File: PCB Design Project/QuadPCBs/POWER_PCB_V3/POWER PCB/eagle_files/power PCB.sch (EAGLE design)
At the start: 33 parts, among them U2 LM2678DX-5.0

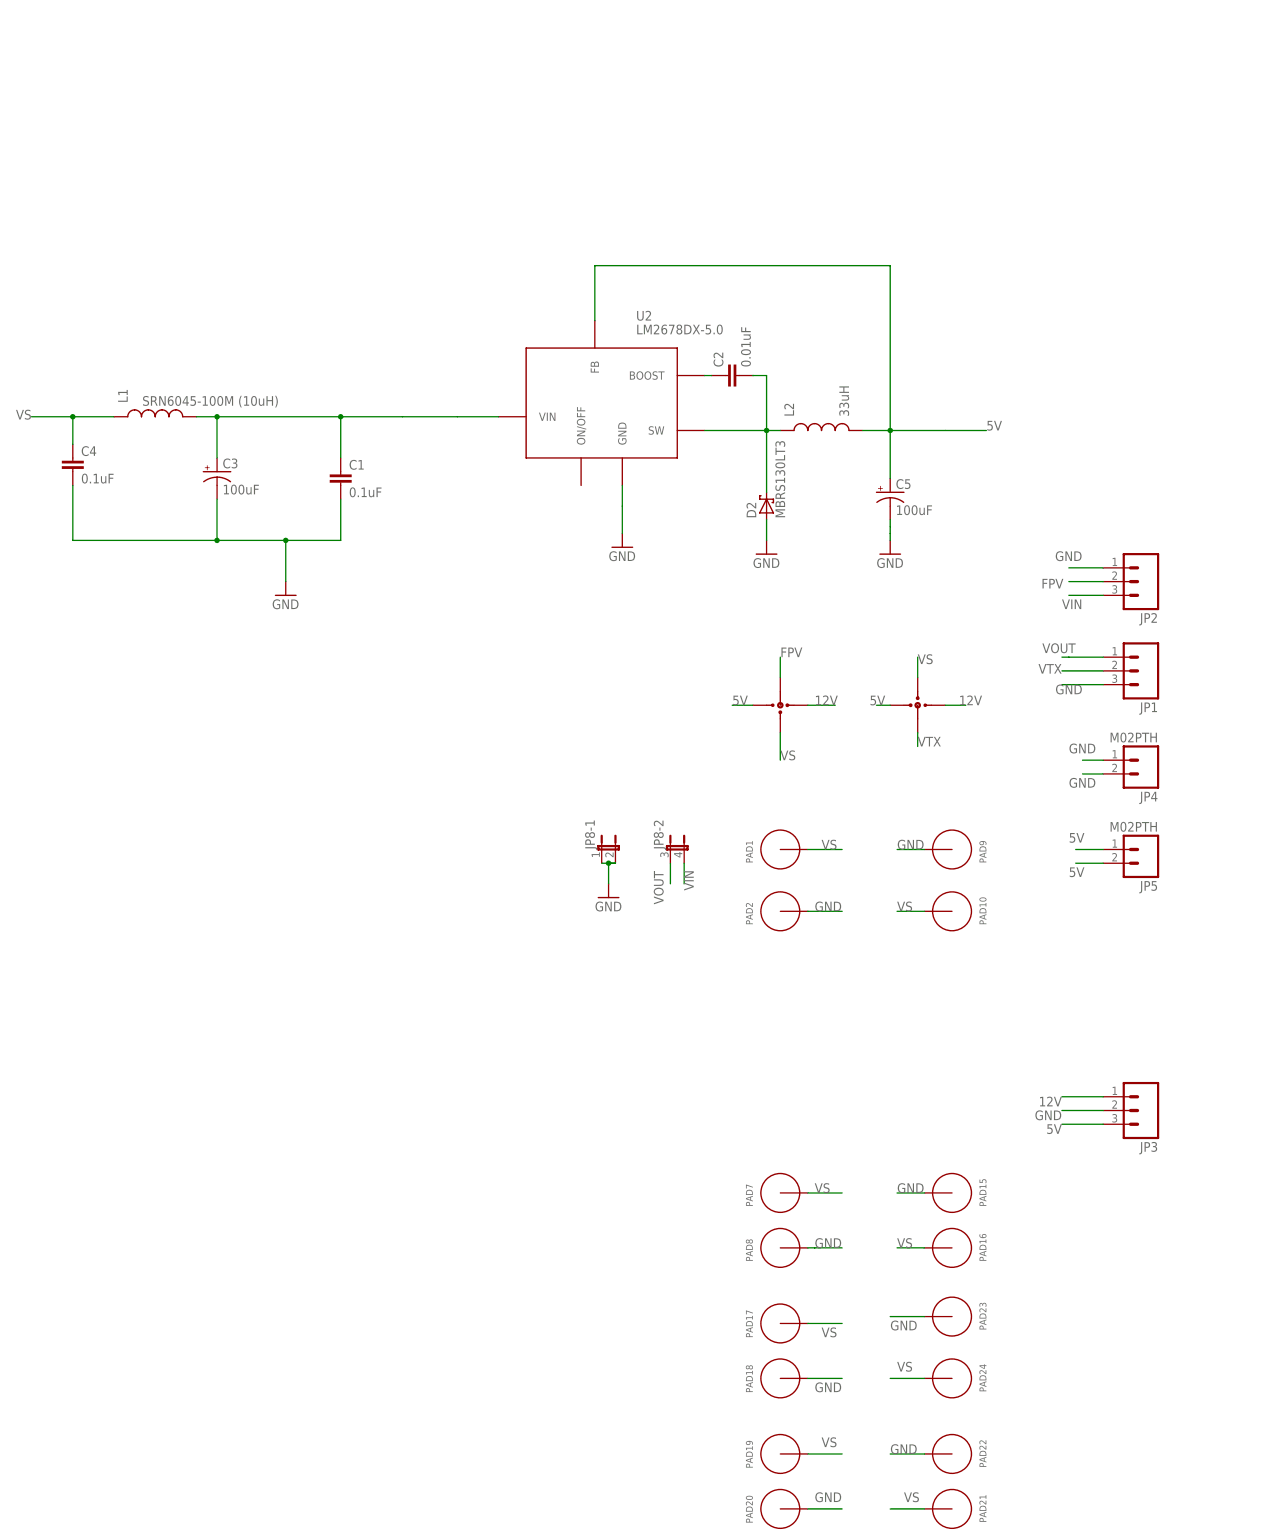
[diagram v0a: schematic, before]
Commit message: modified the Schematic
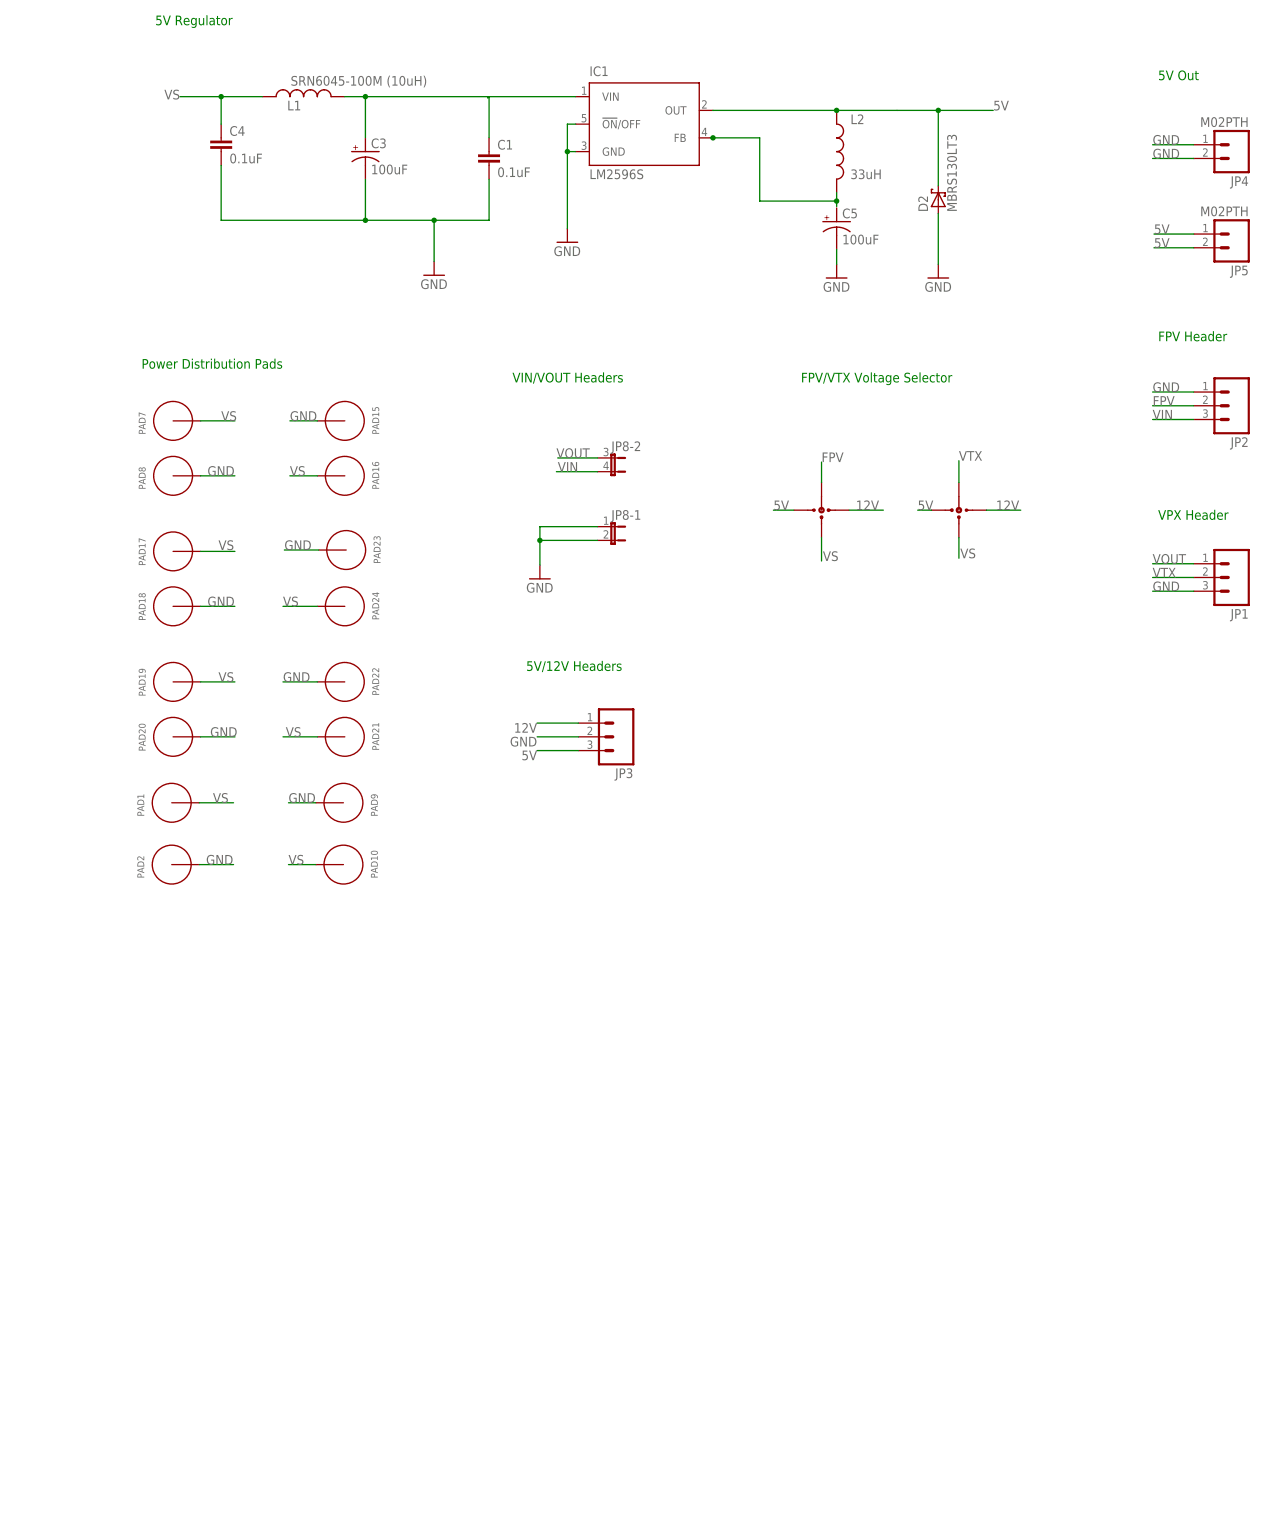
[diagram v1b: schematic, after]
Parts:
- removed C2: 0.01uF, SparkFun-Capacitors:CAP0805
- removed U2: LM2678DX-5.0, LM2678SDX-5.0:LM2678DX-5.0
- added IC1: LM2596S, national-semiconductor:LM2596S
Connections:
- new net N$2: IC1.VIN
- net 5V: now also D2.C; no longer C5.+, L2.2, U2.FB
- net GND: now also IC1.!ON!/OFF, IC1.GND; no longer U2.GND
- net N$1: now also IC1.OUT; no longer C2.2, D2.C, U2.SW
- net N$3: now also IC1.FB, L2.2; no longer C2.1, U2.BOOST
- net N$4: no longer U2.VIN
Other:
- note added: "5V Out"
- note added: "5V Regulator"
- note added: "5V/12V Headers"
- note added: "FPV Header"
- note added: "FPV/VTX Voltage Selector"
- note added: "Power Distribution Pads"
- note added: "VIN/VOUT Headers"
- note added: "VPX Header"
- moved on the sheet: C1, C3, C4, C5, D2, JP1, JP2, JP3, JP4, JP5, JP8-1, JP8-2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

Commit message: layout of component
problem with input cap for the switching regulator
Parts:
- removed C5: 100uF, SparkFun-Capacitors:100UF-10V-10%(TANT)
- removed D2: MBRS130LT3, diode:MBRS130LT3
- removed PAD17, PAD18, PAD19, PAD20, PAD21, PAD22, PAD23, PAD24: PAD_3MM, PAD_3MM:PAD_3MM
- removed U$1, U$3: 3WAY_SMD_JUMPER, jumper_smd_3way:3WAY_SMD_JUMPER
- added C2: 680uF, SparkFun-Capacitors:100UF-10V-10%(TANT)
- added D1: MBRS360, diode:MBRS130LT3
- added JP6: M02PTH, SparkFun-Connectors:M02PTH
- added JP7: (no value), SparkFun-Connectors:M03PTH
- added PAD11, PAD12, PAD13, PAD14, PAD3, PAD4, PAD5, PAD6: PAD_3MM, Power PCB:PAD_3MM
- C1: PROD_ID (none) -> CAP-00810; VALUE (none) -> 0.1uF
- C3: value 100uF -> 0.1uF; device SparkFun-Capacitors:100UF-10V-10%(TANT) -> SparkFun-Capacitors:0.1UF-25V(+80/-20%)(0603); PROD_ID CAP-07890 -> (none); VALUE 100uF -> (none)
- C4: value 0.1uF -> 330uF; device SparkFun-Capacitors:0.1UF-25V(+80/-20%)(0603) -> SparkFun-Capacitors:100UF-10V-10%(TANT); PROD_ID CAP-00810 -> (none); VALUE 0.1uF -> (none)
- JP1: device SparkFun-Connectors:M03PTH -> jumper:JP2QE
- JP3: value (none) -> 3WAY_SMD_JUMPER; device SparkFun-Connectors:M03PTH -> Power PCB:3WAY_SMD_JUMPER
- JP4: value M02PTH -> 3WAY_SMD_JUMPER; device SparkFun-Connectors:M02PTH -> Power PCB:3WAY_SMD_JUMPER
- JP8: device jumper:JP2QE -> SparkFun-Connectors:M03PTH
- PAD1, PAD10, PAD15, PAD16, PAD2, PAD7, PAD8, PAD9: device PAD_3MM:PAD_3MM -> Power PCB:PAD_3MM
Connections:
- removed net N$1: IC1.OUT, L2.1
- removed net N$2: IC1.VIN
- removed net N$4: C1.1, C3.+, L1.2
- new net VSF: C2.+, C3.1, IC1.VIN, JP3.2, JP4.2, L1.2
- net 12V: now also JP2.1, JP3.3, JP4.1; no longer JP3.1, U$1.3, U$3.1
- net 5V: now also C4.+, IC1.FB, JP2.3, JP3.1, JP4.3, JP6.1, JP6.2, L2.2; no longer D2.C, JP3.3, JP5.1, JP5.2, U$1.1, U$3.3
- net FPV: now also JP3.4, JP7.2; no longer JP2.2, U$1.4
- net GND: now also C2.-, C3.2, C4.-, D1.A, JP1-1.1, JP1-1.2, JP2.2, JP5.1, JP5.2, JP7.1, JP8.3, PAD11.1, PAD14.1, PAD16.1, PAD4.1, PAD6.1; no longer C3.-, C4.2, C5.-, D2.A, JP1.3, JP2.1, JP3.2, JP4.1, JP4.2, JP8-1.1, JP8-1.2, PAD15.1, PAD18.1, PAD20.1, PAD22.1, PAD23.1
- net N$3: now also D1.C, IC1.OUT, L2.1; no longer IC1.FB, L2.2
- net VIN: now also JP1-2.2, JP7.3; no longer JP2.3, JP8-2.2
- net VOUT: now also JP1-2.1, JP8.1; no longer JP1.1, JP8-2.1
- net VS: now also C1.1, PAD12.1, PAD13.1, PAD15.1, PAD3.1, PAD5.1; no longer C4.1, PAD16.1, PAD17.1, PAD19.1, PAD21.1, PAD24.1, U$1.2, U$3.2
- net VTX: now also JP4.4, JP8.2; no longer JP1.2, U$3.4
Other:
- moved on the sheet: C1, JP2, JP5, L2, PAD15, PAD16, PAD7, PAD8

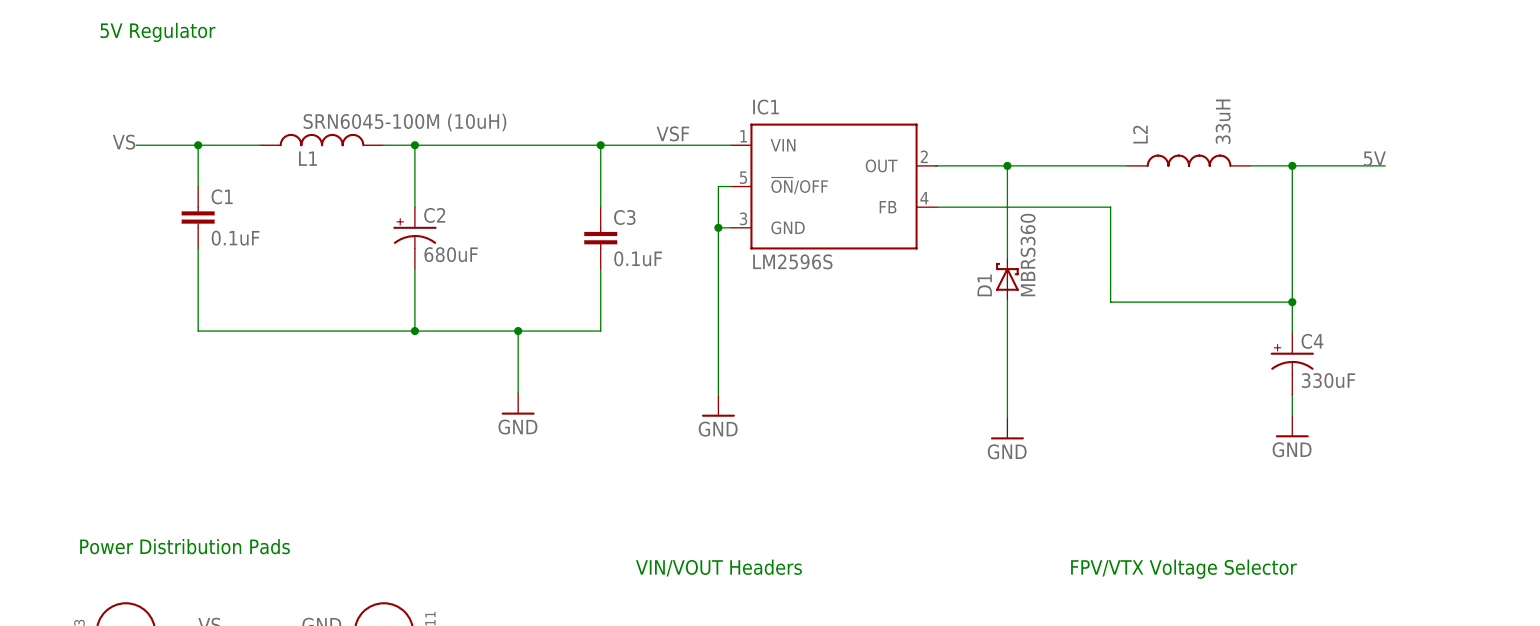
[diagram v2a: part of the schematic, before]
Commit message: finished PCB design
Change regulator back to LM7689 but in TO-203-7 package
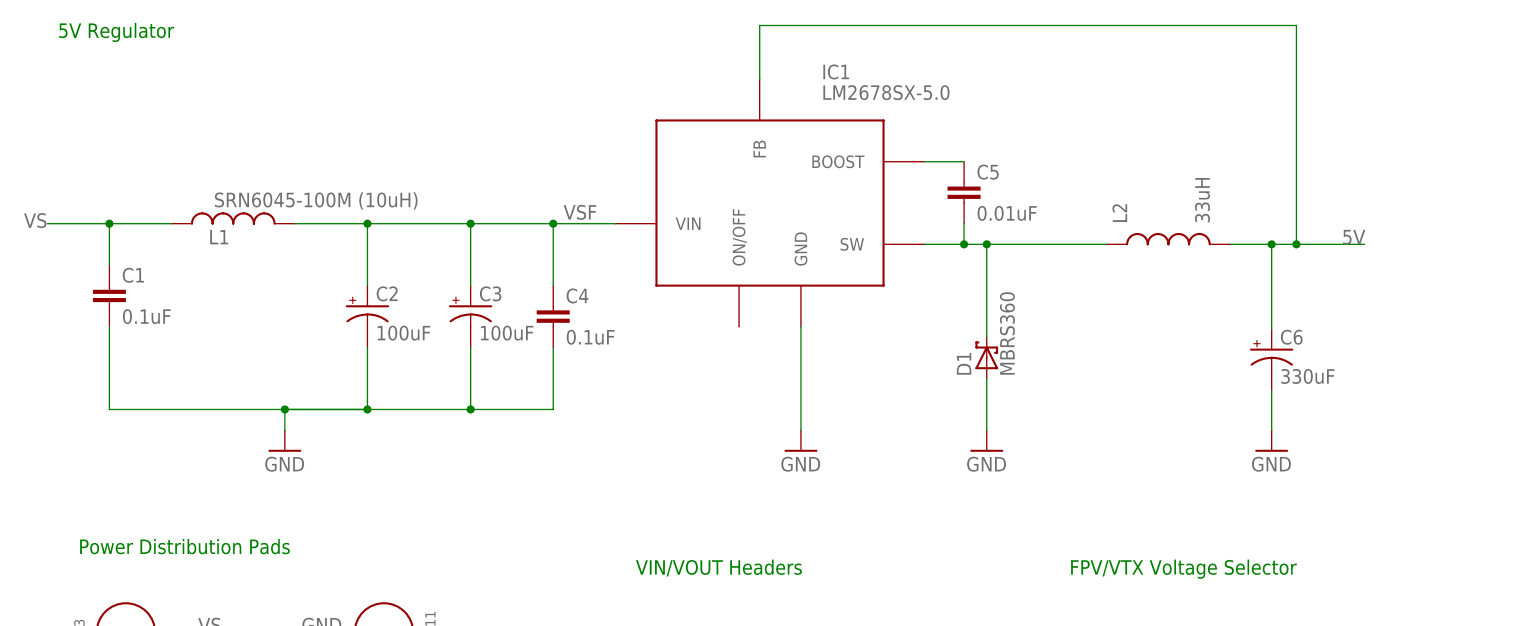
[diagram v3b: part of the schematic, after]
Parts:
- added C5: 0.01uF, SparkFun-Capacitors:0.1UF-25V(+80/-20%)(0603)
- added C6: 330uF, SparkFun-Capacitors:100UF-10V-10%(TANT)
- C2: value 680uF -> 100uF; device SparkFun-Capacitors:100UF-10V-10%(TANT) -> Power PCB:100UF-10V-10%(TANT); PROD_ID CAP-07890 -> (none)
- C3: value 0.1uF -> 100uF; device SparkFun-Capacitors:0.1UF-25V(+80/-20%)(0603) -> Power PCB:100UF-10V-10%(TANT); VALUE (none) -> 100uF
- C4: value 330uF -> 0.1uF; device SparkFun-Capacitors:100UF-10V-10%(TANT) -> SparkFun-Capacitors:0.1UF-25V(+80/-20%)(0603)
- IC1: value LM2596S -> LM2678SX-5.0; device national-semiconductor:LM2596S -> Power PCB:LM2678DX-5.0SX-5.0
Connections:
- new net N$1: C5.1, IC1.BOOST
- net 5V: now also C6.+; no longer C4.+
- net GND: now also C3.-, C4.2, C6.-; no longer C3.2, C4.-, IC1.!ON!/OFF
- net N$3: now also C5.2, IC1.SW; no longer IC1.OUT
- net VSF: now also C3.+, C4.1; no longer C3.1
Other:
- moved on the sheet: C1, D1, L1, L2
